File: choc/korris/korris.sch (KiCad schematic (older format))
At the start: 91 parts

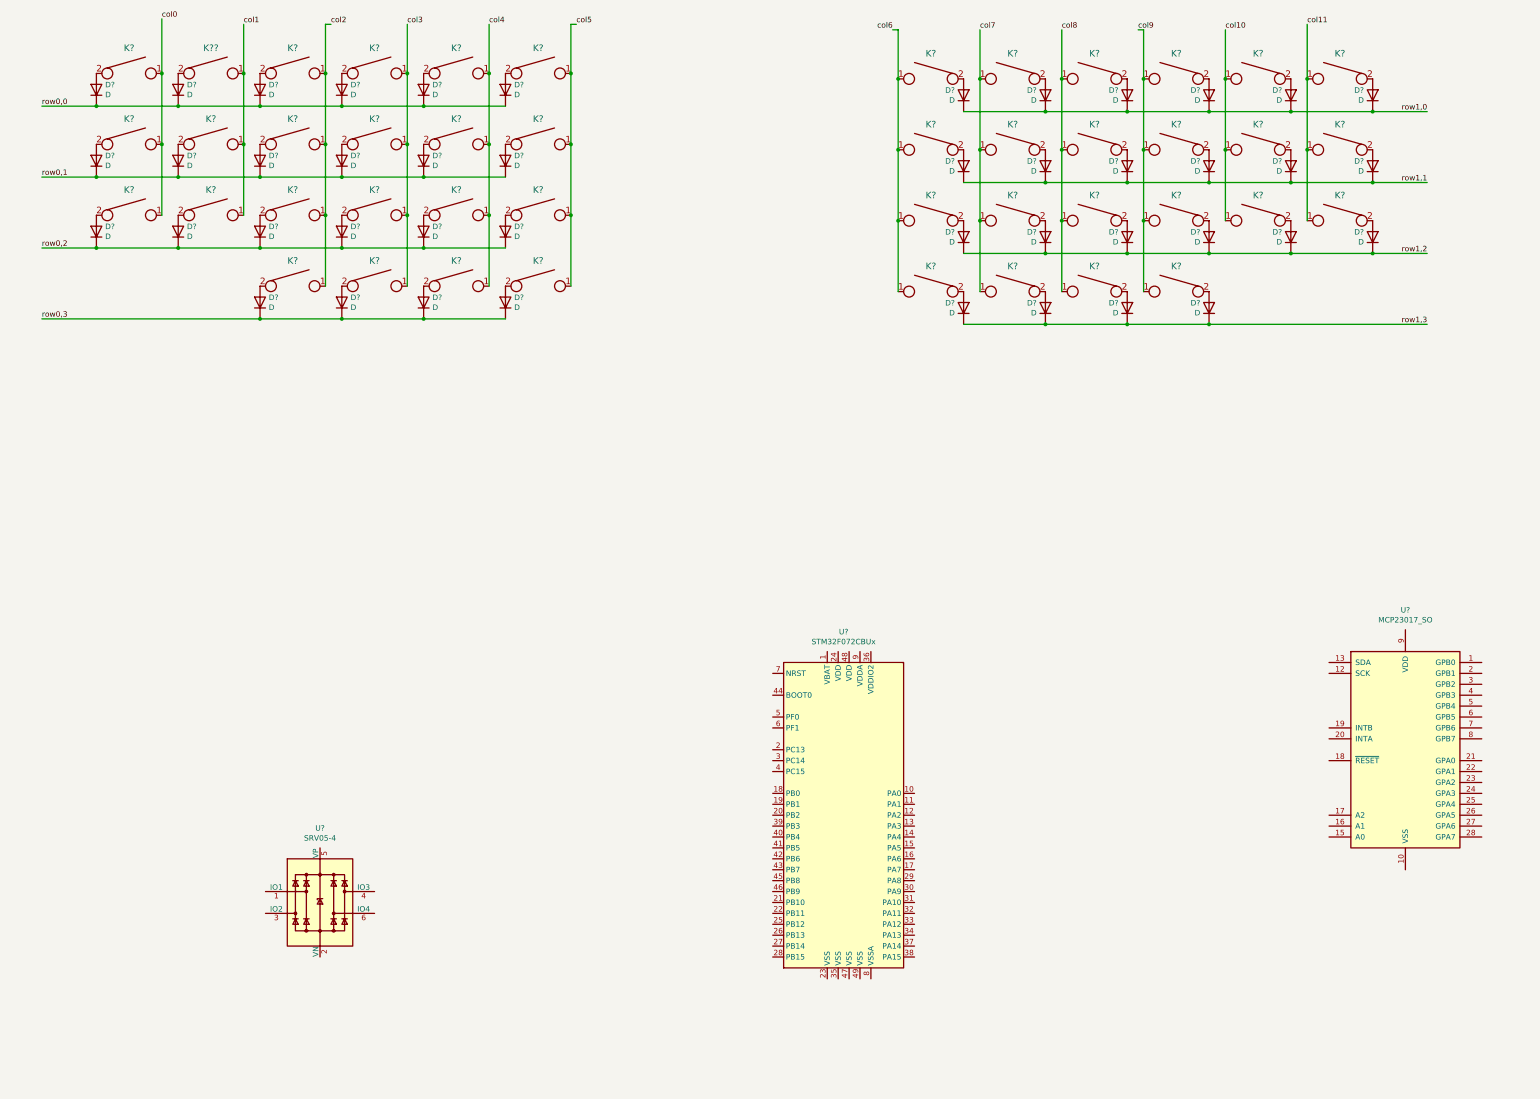
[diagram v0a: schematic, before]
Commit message: layout switches
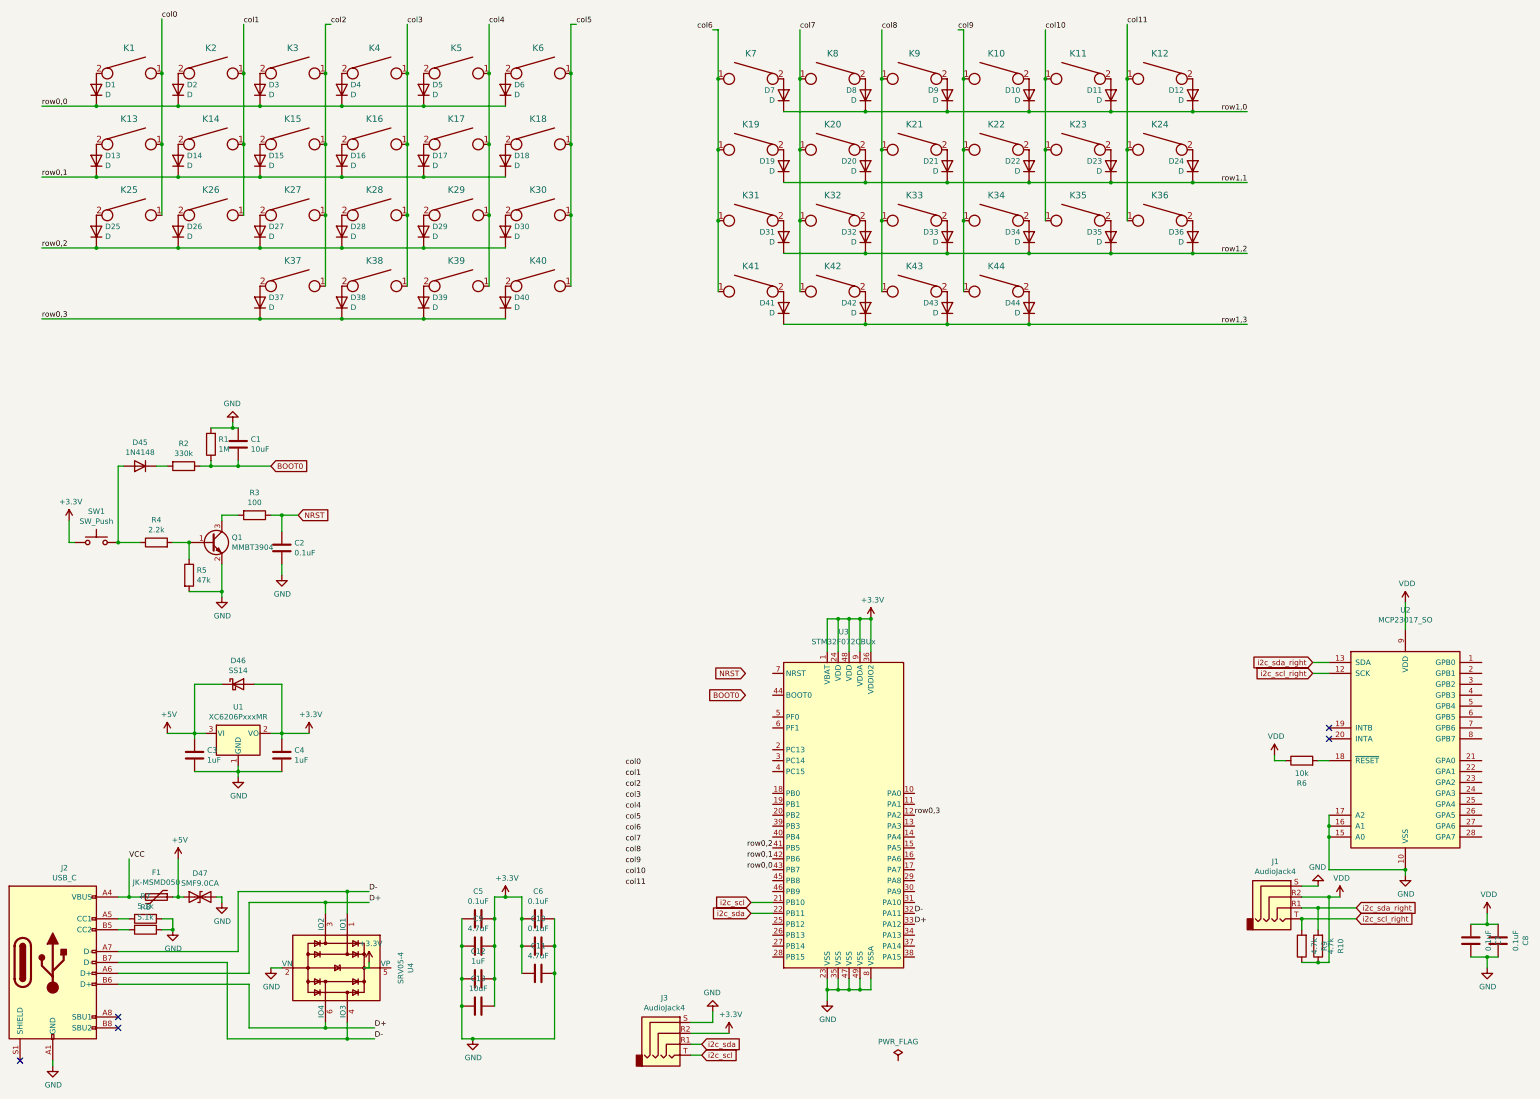
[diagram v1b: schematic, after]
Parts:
- added C1, C13: 10uF, Capacitor_SMD:C_0603_1608Metric, symbol Device:C
- added C10, C2, C5, C6, C7, C8: 0.1uF, Capacitor_SMD:C_0603_1608Metric, symbol Device:C
- added C11, C9: 4.7uF, Capacitor_SMD:C_0603_1608Metric, symbol Device:C
- added C12, C3, C4: 1uF, Capacitor_SMD:C_0603_1608Metric, symbol Device:C
- added D45: 1N4148, Diode_SMD:D_SOD-123, symbol Device:D
- added D46: SS14, Diode_SMD:D_SMA, symbol Device:D_Schottky
- added D47: SMF9.0CA, Diode_SMD:D_SOD-123, symbol Device:D_TVS
- added F1: JK-MSMD050, Fuse:Fuse_1812_4532Metric, symbol Device:Polyfuse
- added J1, J3: AudioJack4, Keebio-Parts:TRRS-PJ-320A, symbol Connector:AudioJack4
- added J2: USB_C, Connector_USB:USB_C_Receptacle_HRO_TYPE-C-31-M-12, symbol Connector:USB_C_Receptacle_USB2.0
- added Q1: MMBT3904, Package_TO_SOT_SMD:SOT-23, symbol Transistor_BJT:MMBT3904
- added R1: 1M, Resistor_SMD:R_0603_1608Metric, symbol Device:R
- added R10, R9: 4.7k, Resistor_SMD:R_0603_1608Metric, symbol Device:R
- added R2: 330k, Resistor_SMD:R_0603_1608Metric, symbol Device:R
- added R3: 100, Resistor_SMD:R_0603_1608Metric, symbol Device:R
- added R4: 2.2k, Resistor_SMD:R_0603_1608Metric, symbol Device:R
- added R5: 47k, Resistor_SMD:R_0603_1608Metric, symbol Device:R
- added R6: 10k, Resistor_SMD:R_0603_1608Metric, symbol Device:R
- added R7, R8: 5.1k, Resistor_SMD:R_0603_1608Metric, symbol Device:R
- added SW1: SW_Push, Button_Switch_SMD:SW_SPST_B3U-1000P, symbol Switch:SW_Push
- added U1: XC6206PxxxMR, Package_TO_SOT_SMD:SOT-23, symbol Regulator_Linear:XC6206PxxxMR
- D1, D10, D11, D12, D13, D14, D15, D16, D17, D18, D19, D2, D20, D21, D22, D23, D24, D25, D26, D27, D28, D29, D3, D30, D31, D32, D33, D34, D35, D36, D37, D38, D39, D4, D40, D41, D42, D43, D44, D5, D6, D7, D8, D9: renamed from D?; footprint (none) -> Diode_SMD:D_SOD-123; LCSC Part (none) -> C81598
- K1, K10, K11, K12, K13, K14, K15, K16, K17, K18, K19, K20, K21, K22, K23, K24, K25, K26, K27, K28, K29, K3, K30, K31, K32, K33, K34, K35, K36, K37, K38, K39, K4, K40, K41, K42, K43, K44, K5, K6, K7, K8, K9: renamed from K?; footprint (none) -> switches:Choc_PG1350_Choc_Spacing
- K2: renamed from K??; footprint (none) -> switches:Choc_PG1350_Choc_Spacing
- U2: renamed from U?; Field4 (none) -> ext
- U3: renamed from U?; url (none) -> https://jlcpcb.com/parts/componentSearch?searchTxt=C92504
- U4: renamed from U?; LCSC Part (none) -> C85364
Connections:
- net row0,0: now also U3.43 (PB7)
- net row0,1: now also U3.42 (PB6)
- net row0,2: now also U3.41 (PB5)
- net row0,3: now also U3.12 (PA2)
- net +3V3: now reaches U3.1 (VBAT)
- net +3V3: now also U3.24 (VDD), U3.36 (VDDIO2), U3.48 (VDD), U3.9 (VDDA), C10.2, C11.2, C12.1, C13.1, C4.2, C5.1, C6.2, C9.1, D46.2 (A), J3.R2, SW1.1, U1.2 (VO)
- net i2c_scl: now reaches U3.21 (PB10)
- net i2c_scl: now also J3.T
- net i2c_sda: now reaches U3.22 (PB11)
- net i2c_sda: now also J3.R1
- net GND: now reaches U3.23 (VSS)
- net GND: now also U2.10 (VSS), U2.15 (A0), U2.16 (A1), U2.17 (A2), U3.35 (VSS), U3.47 (VSS), U3.49 (VSS), U3.8 (VSSA), U4.2 (VN), C1.2, C10.1, C11.1, C12.2, C13.2, C2.1, C3.1, C4.1, C5.2, C6.1, C7.1, C8.1, C9.2, D47.2 (A2), J1.S, J2.A1 (GND), J2.A12 (GND), J2.B1 (GND), J2.B12 (GND), J3.S, Q1.2 (E), R1.2, R5.2, R7.1, R8.1, U1.1 (GND)
- net D-: now reaches U3.32 (PA11)
- net D-: now also U4.1 (IO1), U4.4 (IO3), J2.A7 (D-), J2.B7 (D-)
- net D+: now reaches U3.33 (PA12)
- net D+: now also U4.3 (IO2), U4.6 (IO4), J2.A6 (D+), J2.B6 (D+)
- net i2c_scl_right: now reaches U2.12 (SCK)
- net i2c_scl_right: now also J1.T, R9.2
- net i2c_sda_right: now reaches U2.13 (SDA)
- net i2c_sda_right: now also J1.R1, R10.2
- net at U2.18 (~RESET~): now also R6.2
- net VDD: now reaches U2.9 (VDD)
- net VDD: now also C7.2, C8.2, J1.R2, R10.1, R6.1, R9.1
- new net: D45.2 (A), R4.1, SW1.2
- new net: D45.1 (K), R2.2
- new net: Q1.1 (B), R4.2, R5.1
- new net: Q1.3 (C), R3.2
- new net: J2.A5 (CC1), R7.2
- new net: J2.B5 (CC2), R8.2
- new net +5V: C3.2, D46.1 (K), D47.1 (A1), F1.1, U1.3 (VI)
- new net BOOT0: C1.1, R1.1, R2.1
- new net NRST: C2.2, R3.1
- new net VCC: F1.2, J2.A4 (VBUS), J2.A9 (VBUS), J2.B4 (VBUS), J2.B9 (VBUS)
- no-connect marks 0 -> 5
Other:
- moved on the sheet: D10, D11, D12, D19, D20, D21, D22, D23, D24, D31, D32, D33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

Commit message: add outline for choc layout
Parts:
- added SW2, SW3: Rotary_Encoder_Switch, Keebio-Parts:RotaryEncoder_EC11, symbol Device:Rotary_Encoder_Switch
- J1, J3: footprint Keebio-Parts:TRRS-PJ-320A -> hy-keebs:TRRS-PJ-320Atrrs
- J2: footprint Connector_USB:USB_C_Receptacle_HRO_TYPE-C-31-M-12 -> hy-keebs:USB_C_HRO_TYPE-C-31-M-12
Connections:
- net BOOT0: now also U3.44 (BOOT0)
- net NRST: now also U3.7 (NRST)
- net col0: now also U3.45 (PB8)
- net col1: now also U3.40 (PB4)
- net col10: now also U2.25 (GPA4)
- net col11: now also U2.26 (GPA5)
- net col2: now also U3.39 (PB3)
- net col3: now also U3.38 (PA15)
- net col4: now also U3.37 (PA14)
- net col5: now also U3.34 (PA13)
- net col6: now also U2.21 (GPA0)
- net col7: now also U2.22 (GPA1)
- net col8: now also U2.23 (GPA2)
- net col9: now also U2.24 (GPA3)
- net row1,0: now also U2.1 (GPB0)
- net row1,1: now also U2.2 (GPB1)
- net row1,2: now also U2.3 (GPB2)
- net row1,3: now also U2.4 (GPB3)
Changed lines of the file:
@@
 F 0 "J2" H 1307 10467 50  0000 C CNN
 F 1 "USB_C" H 1307 10376 50  0000 C CNN
-F 2 "Connector_USB:USB_C_Receptacle_HRO_TYPE-C-31-M-12" H 1350 9600 50  0001 C CNN
+F 2 "hy-keebs:USB_C_HRO_TYPE-C-31-M-12" H 1350 9600 50  0001 C CNN
 F 3 "" H 1350 9600 50  0001 C CNN
 F 4 "" H 1200 9600 50  0001 C CNN "LSCS Part"
@@
 F 0 "J3" H 6807 10575 50  0000 C CNN
 F 1 "AudioJack4" H 6807 10484 50  0000 C CNN
-F 2 "Keebio-Parts:TRRS-PJ-320A" H 6850 10250 50  0001 C CNN
+F 2 "hy-keebs:TRRS-PJ-320Atrrs" H 6850 10250 50  0001 C CNN
 F 3 "" H 6850 10250 50  0001 C CNN
 	1    6850 10250
@@
 F 0 "J1" H 12407 9325 50  0000 C CNN
 F 1 "AudioJack4" H 12407 9234 50  0000 C CNN
-F 2 "Keebio-Parts:TRRS-PJ-320A" H 12450 9000 50  0001 C CNN
+F 2 "hy-keebs:TRRS-PJ-320Atrrs" H 12450 9000 50  0001 C CNN
 F 3 "" H 12450 9000 50  0001 C CNN
 	1    12450 9000
@@
 Text Label 9100 8250 0    50   ~ 0
 row0,3
-Text Label 6450 7800 0    50   ~ 0
+Text Label 7800 8850 2    50   ~ 0
 col0
-Text Label 6450 7900 0    50   ~ 0
+Text Label 7800 8450 2    50   ~ 0
 col1
-Text Label 6450 8000 0    50   ~ 0
+Text Label 7800 8350 2    50   ~ 0
 col2
-Text Label 6450 8100 0    50   ~ 0
+Text Label 9100 9550 0    50   ~ 0
 col3
-Text Label 6450 8200 0    50   ~ 0
+Text Label 9100 9450 0    50   ~ 0
 col4
-Text Label 6450 8300 0    50   ~ 0
+Text Label 9100 9350 0    50   ~ 0
 col5
-Text Label 6450 8400 0    50   ~ 0
+Text Label 14300 7750 0    50   ~ 0
 col6
-Text Label 6450 8500 0    50   ~ 0
+Text Label 14300 7850 0    50   ~ 0
 col7
-Text Label 6450 8600 0    50   ~ 0
+Text Label 14300 7950 0    50   ~ 0
 col8
-Text Label 6450 8700 0    50   ~ 0
+Text Label 14300 8050 0    50   ~ 0
 col9
-Text Label 6450 8800 0    50   ~ 0
+Text Label 14300 8150 0    50   ~ 0
 col10
-Text Label 6450 8900 0    50   ~ 0
+Text Label 14300 8250 0    50   ~ 0
 col11
+$Comp
+L Device:Rotary_Encoder_Switch SW2
+U 1 1 607B9801
+P 13650 4450
+F 0 "SW2" H 13650 4817 50  0000 C CNN
+F 1 "Rotary_Encoder_Switch" H 13650 4726 50  0000 C CNN
+F 2 "Keebio-Parts:RotaryEncoder_EC11" H 13500 4610 50  0001 C CNN
+F 3 "" H 13650 4710 50  0001 C CNN
+	1    13650 4450
+	1    0    0    -1
+$EndComp
+$Comp
+L Device:Rotary_Encoder_Switch SW3
+U 1 1 607C274B
+P 13650 5250
+F 0 "SW3" H 13650 5617 50  0000 C CNN
+F 1 "Rotary_Encoder_Switch" H 13650 5526 50  0000 C CNN
+F 2 "Keebio-Parts:RotaryEncoder_EC11" H 13500 5410 50  0001 C CNN
+F 3 "" H 13650 5510 50  0001 C CNN
+	1    13650 5250
+	1    0    0    -1
+$EndComp
+Wire Wire Line
+	7550 6950 7800 6950
+Wire Wire Line
+	7800 7150 7550 7150
+Text Label 14300 6850 0    50   ~ 0
+row1,0
+Text Label 14300 7150 0    50   ~ 0
+row1,3
+Text Label 14300 7050 0    50   ~ 0
+row1,2
+Text Label 14300 6950 0    50   ~ 0
+row1,1
 $EndSCHEMATC

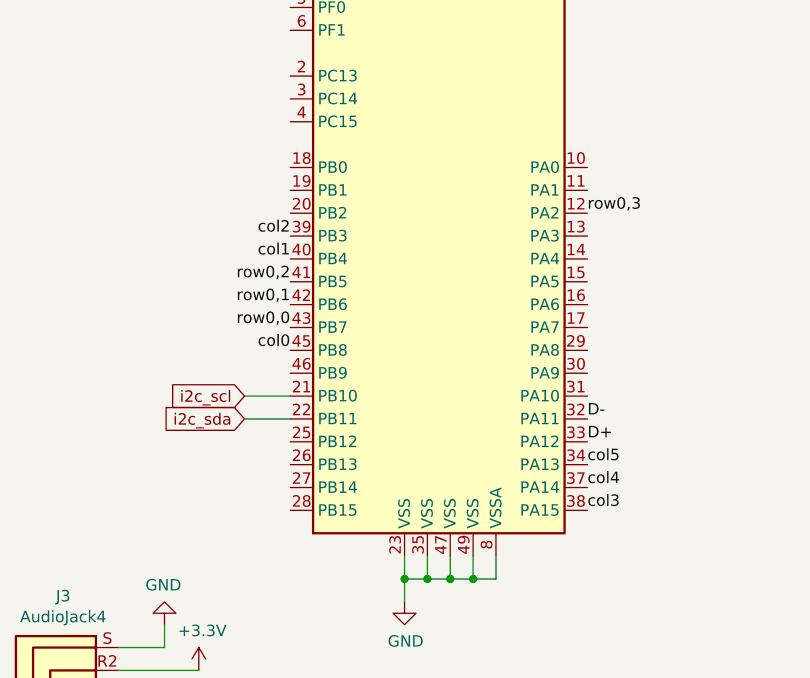
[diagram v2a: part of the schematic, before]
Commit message: routed left half
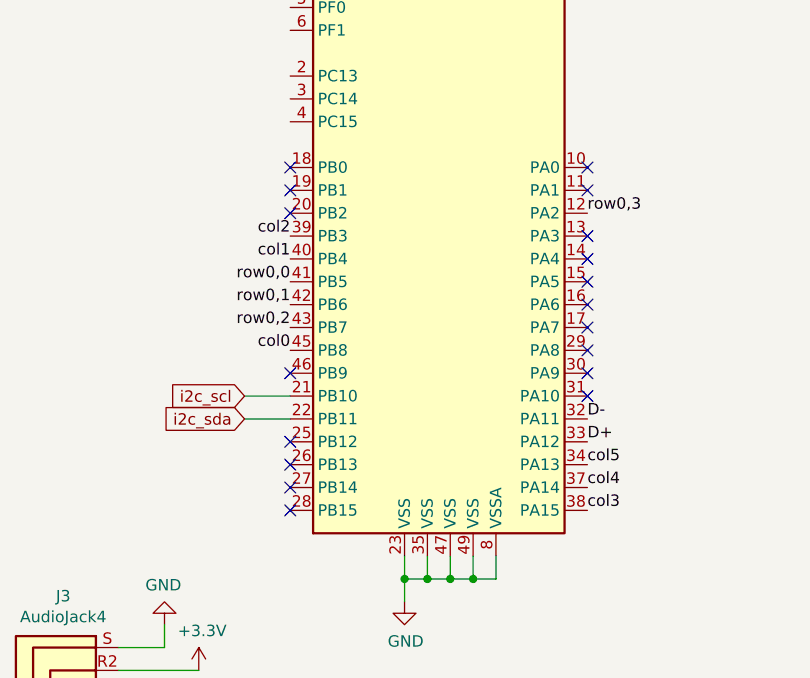
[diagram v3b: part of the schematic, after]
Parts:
- U3: footprint Package_DFN_QFN:QFN-48-1EP_7x7mm_P0.5mm_EP5.6x5.6mm -> breakout_pins:Dual_MCU_QFP_QFN_48_with_breakout_pins
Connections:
- net row0,0: now also U3.41 (PB5); no longer U3.43 (PB7)
- net row0,2: now also U3.43 (PB7); no longer U3.41 (PB5)
- no-connect marks 5 -> 23
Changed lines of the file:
@@
 F 0 "U3" H 8450 9931 50  0000 C CNN
 F 1 "STM32F072CBUx" H 8450 9840 50  0000 C CNN
-F 2 "Package_DFN_QFN:QFN-48-1EP_7x7mm_P0.5mm_EP5.6x5.6mm" H 7900 6850 50  0001 R CNN
+F 2 "breakout_pins:Dual_MCU_QFP_QFN_48_with_breakout_pins" H 7900 6850 50  0001 R CNN
 F 3 "" H 8500 8250 50  0001 C CNN
 F 4 "C92504" H 8500 8250 50  0001 C CNN "LCSC Part"
@@
 	1    0    0    -1
 $EndComp
-Text Label 7800 8750 2    50   ~ 0
+Text Label 7800 8550 2    50   ~ 0
 row0,0
 Text Label 7800 8650 2    50   ~ 0
 row0,1
-Text Label 7800 8550 2    50   ~ 0
+Text Label 7800 8750 2    50   ~ 0
 row0,2
 Text Label 9100 8250 0    50   ~ 0
@@
 Text Label 14300 6950 0    50   ~ 0
 row1,1
+NoConn ~ 9100 8350
+NoConn ~ 9100 8450
+NoConn ~ 9100 8550
+NoConn ~ 9100 8650
+NoConn ~ 9100 8750
+NoConn ~ 9100 8850
+NoConn ~ 9100 8950
+NoConn ~ 9100 9050
+NoConn ~ 9100 8050
+NoConn ~ 9100 8150
+NoConn ~ 7800 8050
+NoConn ~ 7800 8150
+NoConn ~ 7800 8250
+NoConn ~ 7800 8950
+NoConn ~ 7800 9250
+NoConn ~ 7800 9350
+NoConn ~ 7800 9450
+NoConn ~ 7800 9550
 $EndSCHEMATC
